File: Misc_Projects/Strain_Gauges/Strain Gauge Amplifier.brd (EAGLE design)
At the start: 48.3 x 20.3 mm, 17 parts, among them IC1 INS_OPAMP_AD8221, J1 1985218, J3 1985218

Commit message: Added optional headers for strain gauge breakout
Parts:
- added JP2, JP3: (no value), GTOR - Connectors:1X04
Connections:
- net 5V: now also JP2.1, JP3.1
- net A+: now also JP2.2
- net A-: now also JP2.4
- net GND: now also JP2.3, JP3.3
- net VOUT: now also JP3.2
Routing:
- net 5V: track 54.5 -> 71.6 mm
- net GND: track 29.6 -> 38.4 mm
- net A-: track 53.8 -> 58.0 mm
- net A+: track 57.8 -> 61.2 mm
- net VOUT: track 24.9 -> 28.3 mm
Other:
- board text added: "TOP: NC, GND, VOUT, 5V :BOT"
- board text removed: "TOP: 5V, VOUT, GND, NC :BOT"
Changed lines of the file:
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@@
 <layer number="43" name="vRestrict" color="2" fill="10" visible="no" active="yes"/>
 <layer number="44" name="Drills" color="7" fill="1" visible="no" active="yes"/>
-<layer number="45" name="Holes" color="7" fill="1" visible="no" active="yes"/>
+<layer number="45" name="Holes" color="7" fill="1" visible="yes" active="yes"/>
 <layer number="46" name="Milling" color="3" fill="1" visible="no" active="yes"/>
 <layer number="47" name="Measures" color="7" fill="1" visible="no" active="yes"/>
@@
 <wire x1="0" y1="20.32" x2="0" y2="0" width="0" layer="20"/>
 <text x="2.2225" y="19.05" size="0.6096" layer="25">TOP: 5V, A+, GND, A- :BOT</text>
-<text x="34.925" y="19.05" size="0.6096" layer="25">TOP: 5V, VOUT, GND, NC :BOT</text>
+<text x="34.925" y="19.05" size="0.6096" layer="25">TOP: NC, GND, VOUT, 5V :BOT</text>
 <text x="29.5275" y="13.6525" size="1.016" layer="25">R</text>
 <text x="29.5275" y="11.1125" size="1.016" layer="25">G</text>
@@
 <attribute name="VALUE" x="29.21" y="15.24" size="1.27" layer="27" rot="R270"/>
 </element>
+<element name="JP2" library="GTOR - Connectors" package="1X04" package3d_urn="urn:adsk.eagle:package:22407/2" value="" x="2.54" y="10.16" smashed="yes" rot="R270">
+<attribute name="NAME" x="4.3688" y="15.3162" size="1.27" layer="25" ratio="10" rot="R270"/>
+<attribute name="POPULARITY" value="91" x="2.54" y="10.16" size="1.778" layer="27" rot="R270" display="off"/>
+<attribute name="VALUE" x="-0.635" y="15.24" size="1.27" layer="27" rot="R270"/>
+</element>
+<element name="JP3" library="GTOR - Connectors" package="1X04" package3d_urn="urn:adsk.eagle:package:22407/2" value="" x="45.72" y="10.16" smashed="yes" rot="R90">
+<attribute name="NAME" x="43.8912" y="5.0038" size="1.27" layer="25" ratio="10" rot="R90"/>
+<attribute name="POPULARITY" value="91" x="45.72" y="10.16" size="1.778" layer="27" rot="R90" display="off"/>
+<attribute name="VALUE" x="48.895" y="5.08" size="1.27" layer="27" rot="R90"/>
+</element>
 </elements>
 <signals>
@@
 <wire x1="5.87375" y1="10.95375" x2="5.795" y2="11.105" width="0.1524" layer="16"/>
 <via x="13.49375" y="14.76375" extent="1-16" drill="0.35"/>
+<contactref element="JP2" pad="2"/>
+<wire x1="2.54" y1="11.43" x2="5.47" y2="11.43" width="0.1524" layer="1"/>
+<wire x1="5.47" y1="11.43" x2="5.795" y2="11.105" width="0.1524" layer="1"/>
 </signal>
 <signal name="A-">
@@
 <wire x1="21.2725" y1="14.2875" x2="21.27" y2="14.31" width="0.1524" layer="1"/>
 <via x="23.97125" y="14.2875" extent="1-16" drill="0.35"/>
+<contactref element="JP2" pad="4"/>
+<wire x1="2.54" y1="6.35" x2="3.55" y2="6.35" width="0.1524" layer="1"/>
+<wire x1="3.55" y1="6.35" x2="5.795" y2="4.105" width="0.1524" layer="1"/>
 </signal>
 <signal name="5V">
@@
 <wire x1="23.0175" y1="12.38125" x2="23.0175" y2="10.4775" width="0.1524" layer="1"/>
 <wire x1="25.87625" y1="15.24" x2="23.0175" y2="12.38125" width="0.1524" layer="1"/>
+<contactref element="JP2" pad="1"/>
+<contactref element="JP3" pad="1"/>
+<wire x1="2.54" y1="13.97" x2="3.175" y2="14.605" width="0.1524" layer="1"/>
+<wire x1="3.175" y1="14.605" x2="10.795" y2="14.605" width="0.1524" layer="1"/>
+<wire x1="45.72" y1="6.35" x2="45.085" y2="5.715" width="0.1524" layer="16"/>
+<wire x1="45.085" y1="5.715" x2="37.465" y2="5.715" width="0.1524" layer="16"/>
 </signal>
 <signal name="GND">
@@
 <wire x1="28.575" y1="7.9375" x2="28.4175" y2="7.9375" width="0.1524" layer="1"/>
 <via x="20.32" y="2.54" extent="1-16" drill="0.35"/>
+<contactref element="JP2" pad="3"/>
+<contactref element="JP3" pad="3"/>
+<wire x1="45.72" y1="11.43" x2="38.75" y2="11.43" width="0.1524" layer="1"/>
+<wire x1="38.75" y1="11.43" x2="37.465" y2="12.715" width="0.1524" layer="1"/>
 </signal>
 <signal name="N$2">
@@
 <wire x1="25.87625" y1="13.6525" x2="25.72" y2="13.66" width="0.1524" layer="1"/>
 <wire x1="42.38625" y1="9.2075" x2="42.465" y2="9.215" width="0.1524" layer="1"/>
+<contactref element="JP3" pad="2"/>
+<wire x1="45.72" y1="8.89" x2="42.79" y2="8.89" width="0.1524" layer="1"/>
+<wire x1="42.79" y1="8.89" x2="42.465" y2="9.215" width="0.1524" layer="1"/>
 </signal>
 <signal name="N$15">

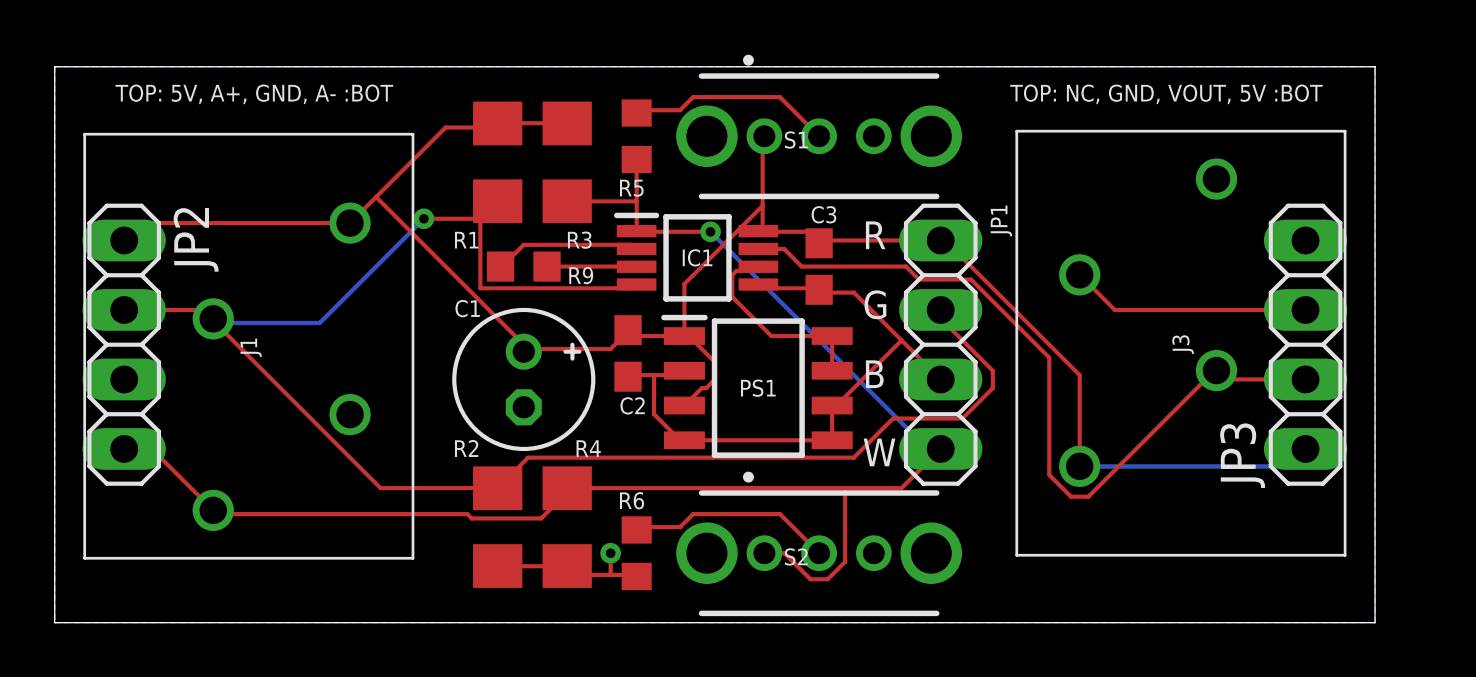
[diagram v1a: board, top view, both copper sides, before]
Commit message: changed connectors on strain gauge amplifier to microfit
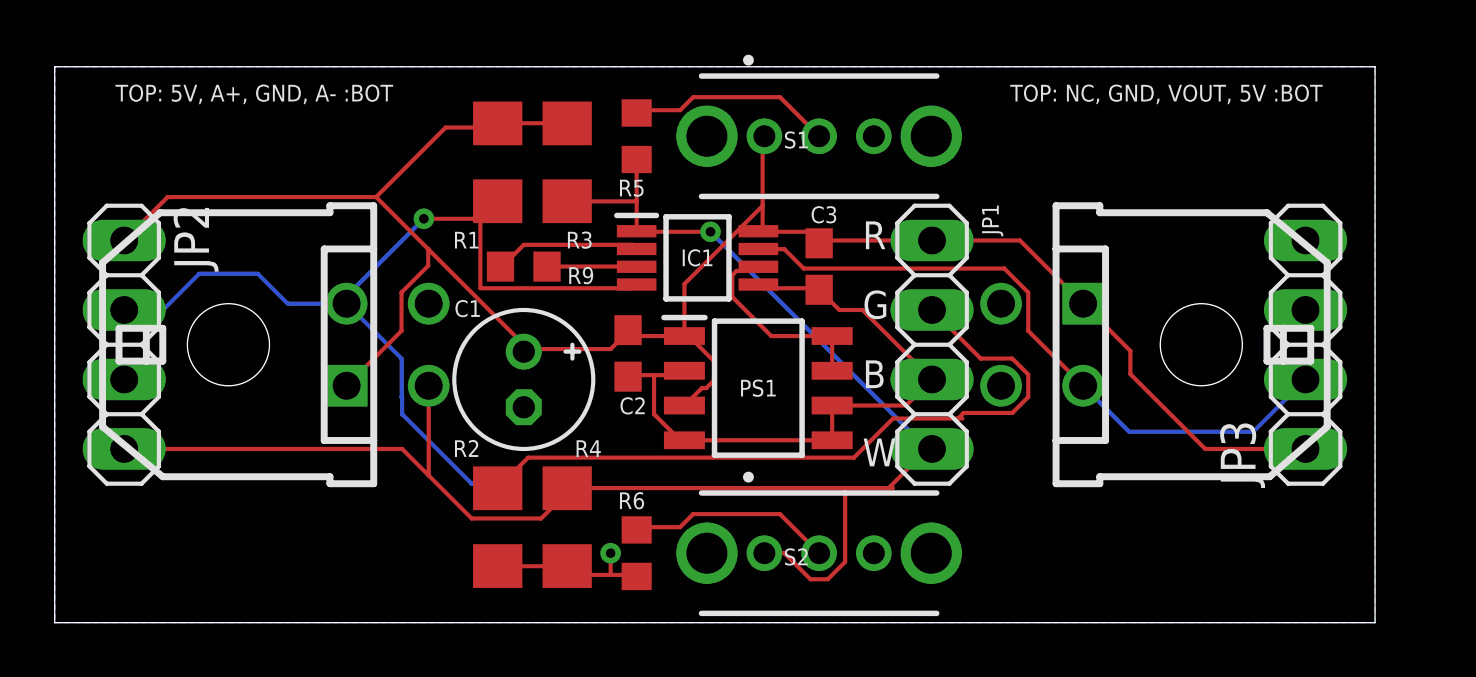
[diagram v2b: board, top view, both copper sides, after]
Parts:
- removed J1, J3: 1985218, GTOR - Connectors:1985218
- added X1, X2: (no value), GTOR - Microfit Connector:43045-0400
- moved JP1 0.32 mm to (32.1, 10.2)
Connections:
- removed net N$15: J3.4
- net 5V: now also X1.P$1, X2.P$1; no longer J1.1, J3.1
- net A+: now also X1.P$2; no longer J1.2
- net A-: now also X1.P$3; no longer J1.4
- net GND: now also X1.P$4, X2.P$4; no longer J1.3, J3.3
- net VOUT: now also X2.P$2; no longer J3.2
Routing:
- net GND: track 38.4 -> 30.0 mm
- net 5V: track 71.6 -> 76.0 mm
- net VOUT: track 28.3 -> 24.4 mm
- net A-: track 58.0 -> 60.6 mm

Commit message: changed strain gauge board connectors to microfit
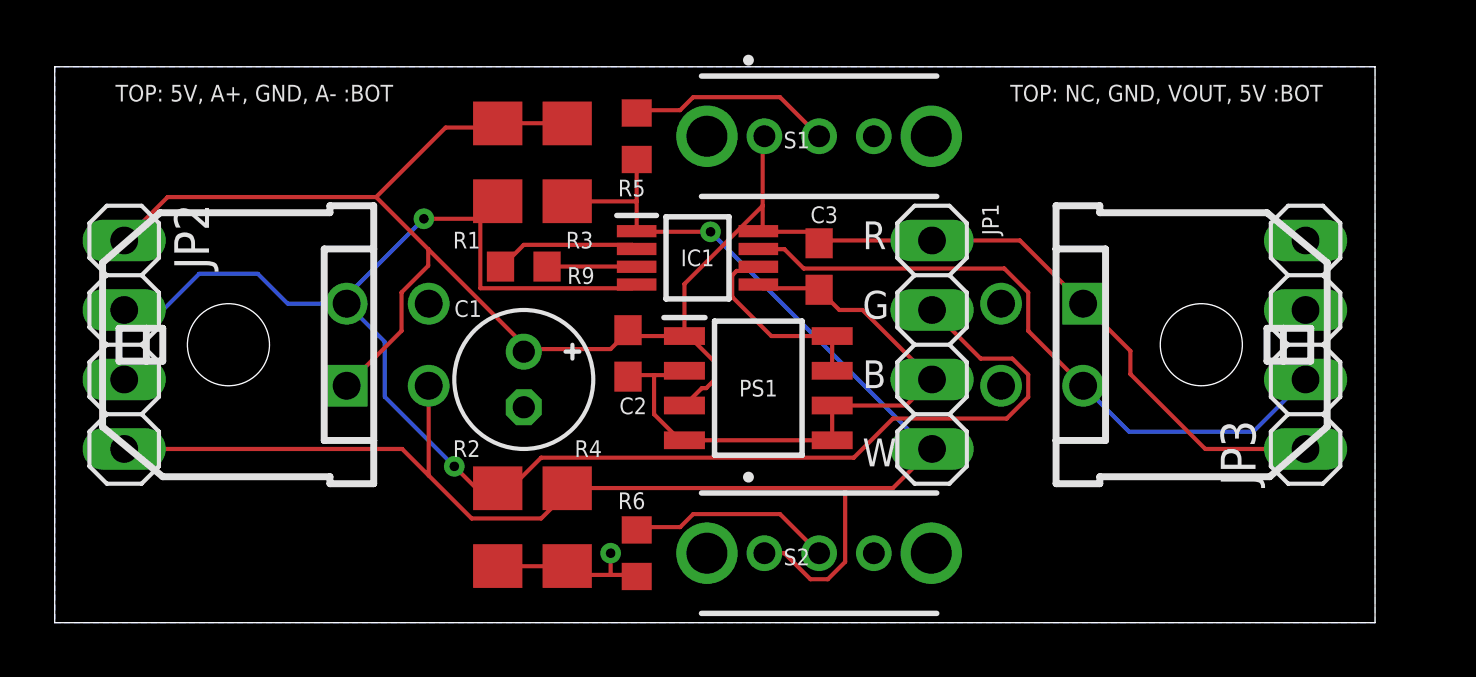
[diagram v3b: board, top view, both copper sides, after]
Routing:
- net A+: track 61.6 -> 61.2 mm, vias 1 -> 2
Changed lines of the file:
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@@
 <wire x1="21.11375" y1="12.22375" x2="21.27" y2="12.36" width="0.1524" layer="1"/>
 <wire x1="16.1925" y1="15.39875" x2="16.1925" y2="15.4055" width="0.1524" layer="1"/>
-<wire x1="30.63875" y1="7.46125" x2="33.02" y2="7.46125" width="0.1524" layer="1"/>
-<wire x1="33.02" y1="7.46125" x2="33.17875" y2="7.46125" width="0.1524" layer="1"/>
-<wire x1="29.21" y1="6.0325" x2="30.63875" y2="7.46125" width="0.1524" layer="1"/>
-<wire x1="17.30375" y1="6.0325" x2="29.21" y2="6.0325" width="0.1524" layer="1"/>
-<wire x1="16.1925" y1="4.92125" x2="17.30375" y2="6.0325" width="0.1524" layer="1"/>
-<wire x1="16.1925" y1="4.92125" x2="16.1925" y2="4.9145" width="0.1524" layer="1"/>
+<wire x1="30.63875" y1="7.46125" x2="29.21" y2="6.0325" width="0.1524" layer="1"/>
+<wire x1="17.78" y1="6.0325" x2="29.21" y2="6.0325" width="0.1524" layer="1"/>
 <wire x1="15.5575" y1="14.76375" x2="16.1925" y2="15.4055" width="0.1524" layer="1"/>
 <contactref element="JP2" pad="2"/>
@@
 <wire x1="10.67" y1="11.66" x2="8.515925" y2="11.66" width="0.1524" layer="16"/>
 <wire x1="8.515925" y1="11.66" x2="7.423725" y2="12.7522" width="0.1524" layer="16"/>
-<wire x1="12.6764" y1="8.24843125" x2="12.7" y2="8.22483125" width="0.1524" layer="16"/>
-<wire x1="12.7" y1="8.22483125" x2="12.7" y2="7.62" width="0.1524" layer="16"/>
-<wire x1="10.67" y1="11.66" x2="12.6764" y2="9.6536" width="0.1524" layer="16"/>
-<wire x1="12.6764" y1="9.6536" x2="12.6764" y2="8.24843125" width="0.1524" layer="16"/>
-<wire x1="12.7" y1="7.62" x2="15.24" y2="5.08" width="0.1524" layer="16"/>
-<wire x1="15.24" y1="5.08" x2="16.51" y2="5.08" width="0.1524" layer="16"/>
-<wire x1="35.00156875" y1="7.6664" x2="35.5836" y2="8.24843125" width="0.1524" layer="1"/>
-<wire x1="35.5836" y1="8.24843125" x2="35.5836" y2="9.07156875" width="0.1524" layer="1"/>
+<wire x1="35.5836" y1="9.07156875" x2="35.5836" y2="8.24843125" width="0.1524" layer="1"/>
 <wire x1="35.5836" y1="9.07156875" x2="35.00156875" y2="9.6536" width="0.1524" layer="1"/>
-<wire x1="33.02" y1="7.46125" x2="33.22515" y2="7.6664" width="0.1524" layer="1"/>
 <wire x1="35.00156875" y1="9.6536" x2="33.8439" y2="9.6536" width="0.1524" layer="1"/>
-<wire x1="33.22515" y1="7.6664" x2="35.00156875" y2="7.6664" width="0.1524" layer="1"/>
 <wire x1="33.8439" y1="9.6536" x2="32.0675" y2="11.43" width="0.1524" layer="1"/>
-<wire x1="16.51" y1="5.08" x2="16.1925" y2="4.9145" width="0" layer="19" extent="1-16"/>
+<wire x1="35.5836" y1="8.24843125" x2="34.79641875" y2="7.46125" width="0.1524" layer="1"/>
+<wire x1="34.79641875" y1="7.46125" x2="30.63875" y2="7.46125" width="0.1524" layer="1"/>
+<wire x1="16.1925" y1="4.9145" x2="16.1925" y2="4.92125" width="0.1524" layer="1"/>
+<wire x1="16.662" y1="4.9145" x2="17.78" y2="6.0325" width="0.1524" layer="1"/>
+<wire x1="16.1925" y1="4.9145" x2="16.51" y2="4.9145" width="0.1524" layer="1"/>
+<wire x1="16.51" y1="4.9145" x2="16.662" y2="4.9145" width="0.1524" layer="1"/>
+<wire x1="10.67" y1="11.66" x2="12.065" y2="10.265" width="0.1524" layer="16"/>
+<wire x1="12.065" y1="10.265" x2="12.065" y2="8.255" width="0.1524" layer="16"/>
+<via x="14.605" y="5.715" extent="1-16" drill="0.35"/>
+<wire x1="15.4055" y1="4.9145" x2="16.1925" y2="4.9145" width="0.1524" layer="1"/>
+<wire x1="12.065" y1="8.255" x2="14.605" y2="5.715" width="0.1524" layer="16"/>
+<wire x1="14.605" y1="5.715" x2="15.4055" y2="4.9145" width="0.1524" layer="1"/>
 </signal>
 <signal name="A-">
@@
 <wire x1="21.2725" y1="15.39875" x2="18.7325" y2="15.39875" width="0.1524" layer="1"/>
 <wire x1="18.7325" y1="15.39875" x2="18.7325" y2="15.4055" width="0.1524" layer="1"/>
-<wire x1="30.63875" y1="4.92125" x2="30.48" y2="4.92125" width="0.1524" layer="1"/>
-<wire x1="30.48" y1="4.92125" x2="28.8925" y2="4.92125" width="0.1524" layer="1"/>
 <wire x1="28.8925" y1="4.92125" x2="18.7325" y2="4.92125" width="0.1524" layer="1"/>
 <wire x1="18.7325" y1="4.92125" x2="18.7325" y2="4.9145" width="0.1524" layer="1"/>
@@
 <wire x1="18.7325" y1="4.7625" x2="18.7325" y2="4.9145" width="0.1524" layer="1"/>
 <wire x1="23.97125" y1="14.2875" x2="21.2725" y2="14.2875" width="0.1524" layer="1"/>
-<wire x1="31.90875" y1="6.35" x2="23.97125" y2="14.2875" width="0.1524" layer="16"/>
 <wire x1="21.2725" y1="14.2875" x2="21.27" y2="14.31" width="0.1524" layer="1"/>
 <via x="23.97125" y="14.2875" extent="1-16" drill="0.35"/>
@@
 <wire x1="2.54" y1="6.35" x2="12.7" y2="6.35" width="0.1524" layer="1"/>
 <wire x1="12.7" y1="6.35" x2="13.67" y2="5.38" width="0.1524" layer="1"/>
-<wire x1="30.48" y1="4.92125" x2="31.90875" y2="6.35" width="0.1524" layer="1"/>
-<wire x1="31.90875" y1="6.35" x2="32.0675" y2="6.35" width="0.1524" layer="1"/>
-<wire x1="32.0675" y1="6.35" x2="31.90875" y2="6.35" width="0" layer="19" extent="16-16"/>
+<wire x1="30.63875" y1="4.92125" x2="32.0675" y2="6.35" width="0.1524" layer="1"/>
+<wire x1="28.8925" y1="4.92125" x2="30.63875" y2="4.92125" width="0.1524" layer="1"/>
+<wire x1="23.97125" y1="14.2875" x2="31.90875" y2="6.35" width="0.1524" layer="16"/>
+<wire x1="31.90875" y1="6.35" x2="32.0675" y2="6.35" width="0.1524" layer="16"/>
 </signal>
 <signal name="5V">
